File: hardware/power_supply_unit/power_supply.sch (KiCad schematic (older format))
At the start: 19 parts, among them U1 LT1074

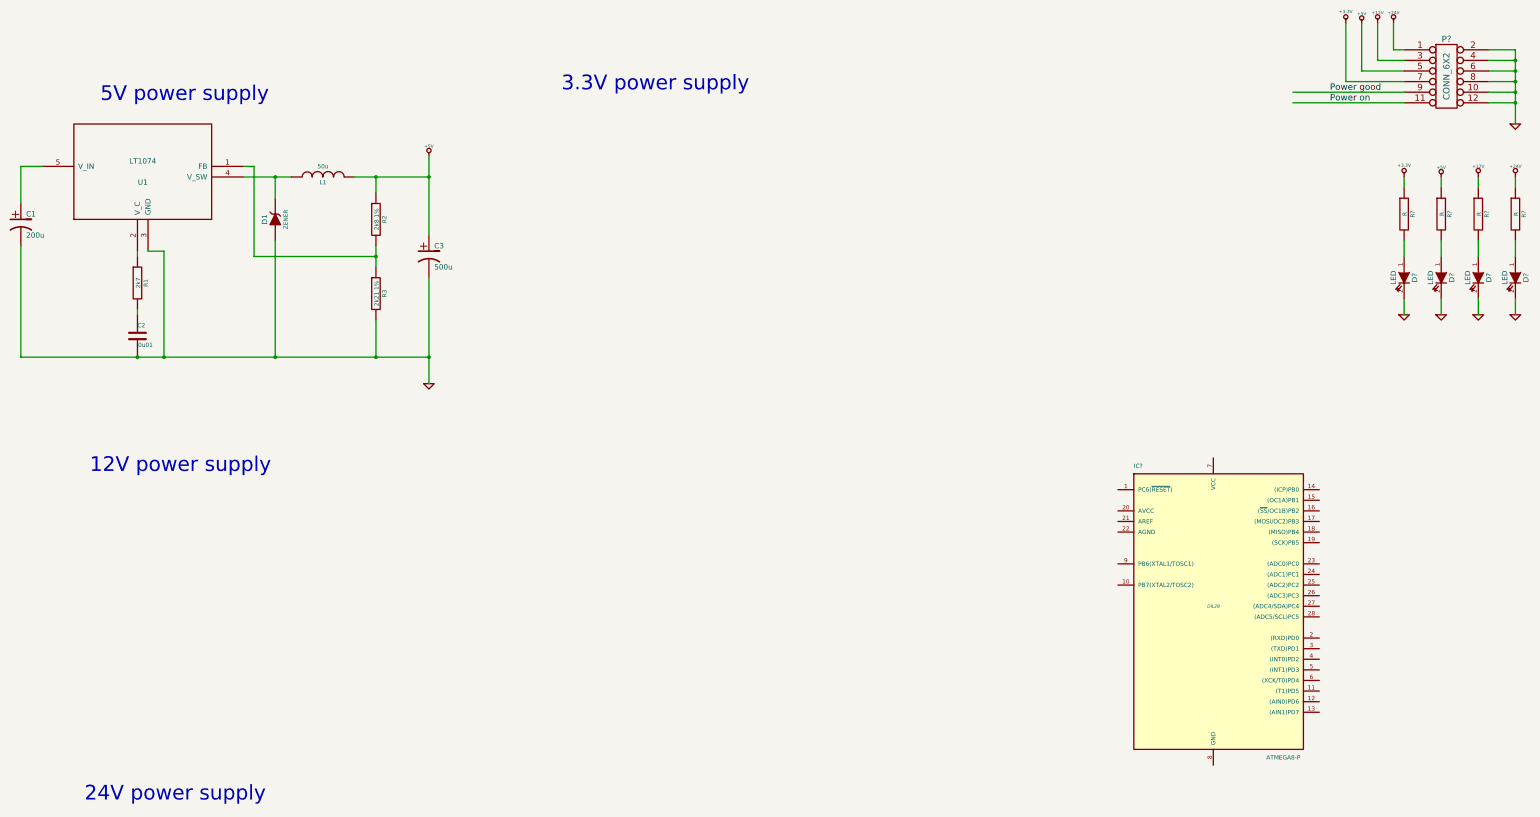
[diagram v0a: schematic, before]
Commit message: Improved digital output card with modbus controller
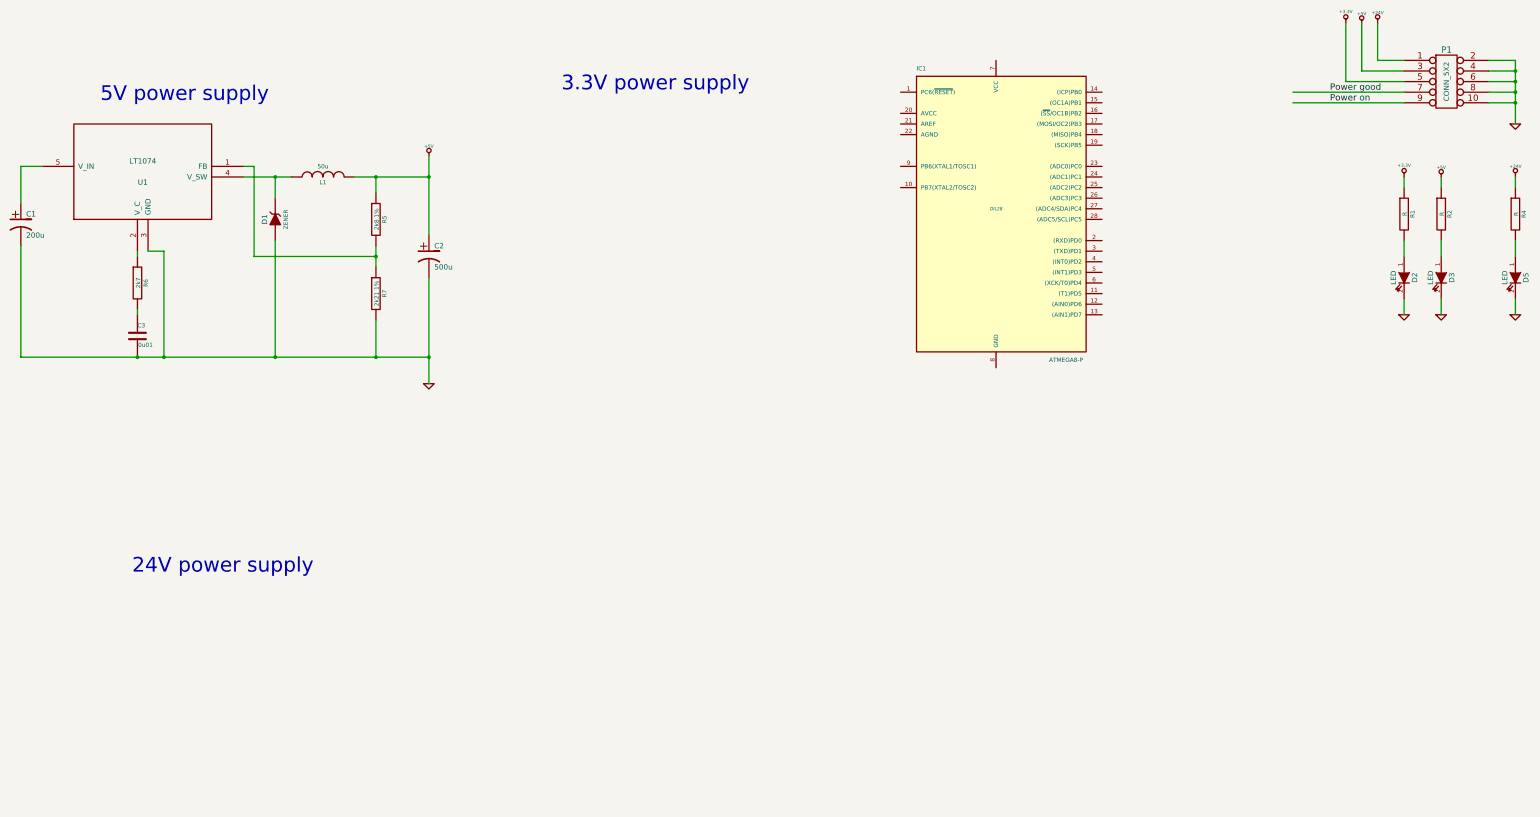
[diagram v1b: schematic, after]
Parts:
- removed D?: LED, ~, symbol LED
- removed P?: CONN_6X2, symbol CONN_6X2
- removed R?: R, ~, symbol R
- added P1: CONN_5X2, symbol CONN_5X2
- gave numbers to parts that had none: 7
- renumbered C3 to C2, C2 to C3, R2 to R5, R1 to R6, R3 to R7
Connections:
- net labels removed: +12V
- wire segments 49 -> 43
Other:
- note removed: "12V power supply"
- moved on the sheet: IC1
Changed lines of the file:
@@
 $EndComp
 $Comp
-L C C2
+L C C3
 U 1 1 5571A0D0
 P 2300 3850
-F 0 "C2" H 2300 3950 40  0000 L CNN
+F 0 "C3" H 2300 3950 40  0000 L CNN
 F 1 "0u01" H 2306 3765 40  0000 L CNN
 F 2 "~" H 2338 3700 30  0000 C CNN
@@
 Connection ~ 2300 4050
 $Comp
-L R R1
+L R R6
 U 1 1 5571A120
 P 2300 3350
-F 0 "R1" V 2380 3350 40  0000 C CNN
+F 0 "R6" V 2380 3350 40  0000 C CNN
 F 1 "2k7" V 2307 3351 40  0000 C CNN
 F 2 "~" V 2230 3350 30  0000 C CNN
@@
 Connection ~ 3600 2350
 $Comp
-L R R2
+L R R5
 U 1 1 5571A333
 P 4550 2750
-F 0 "R2" V 4630 2750 40  0000 C CNN
+F 0 "R5" V 4630 2750 40  0000 C CNN
 F 1 "2k8 1%" V 4557 2751 40  0000 C CNN
 F 2 "~" V 4480 2750 30  0000 C CNN
@@
 $EndComp
 $Comp
-L R R3
+L R R7
 U 1 1 5571A339
 P 4550 3450
-F 0 "R3" V 4630 3450 40  0000 C CNN
+F 0 "R7" V 4630 3450 40  0000 C CNN
 F 1 "2k21 1%" V 4557 3451 40  0000 C CNN
 F 2 "~" V 4480 3450 30  0000 C CNN
@@
 Connection ~ 3600 4050
 $Comp
-L CP1 C3
+L CP1 C2
 U 1 1 5571A3A1
 P 5050 3100
-F 0 "C3" H 5100 3200 50  0000 L CNN
+F 0 "C2" H 5100 3200 50  0000 L CNN
 F 1 "500u" H 5100 3000 50  0000 L CNN
 F 2 "~" H 5050 3100 60  0000 C CNN
@@
 Connection ~ 2550 4050
 $Comp
-L +5V #PWR?
+L +5V #PWR5
 U 1 1 5571A51F
 P 5050 2150
-F 0 "#PWR?" H 5050 2240 20  0001 C CNN
+F 0 "#PWR5" H 5050 2240 20  0001 C CNN
 F 1 "+5V" H 5050 2240 30  0000 C CNN
 F 2 "" H 5050 2150 60  0000 C CNN
@@
 Connection ~ 5050 2350
 $Comp
-L GND #PWR?
+L GND #PWR14
 U 1 1 5571A54A
 P 5050 4300
-F 0 "#PWR?" H 5050 4300 30  0001 C CNN
+F 0 "#PWR14" H 5050 4300 30  0001 C CNN
 F 1 "GND" H 5050 4230 30  0001 C CNN
 F 2 "" H 5050 4300 60  0000 C CNN
@@
 Text Notes 1950 1650 0    139  ~ 0
 5V power supply
-Text Notes 1850 5150 0    139  ~ 0
-12V power supply
-Text Notes 1800 8250 0    139  ~ 0
+Text Notes 2250 6100 0    139  ~ 0
 24V power supply
 Text Notes 6300 1550 0    139  ~ 0
 3.3V power supply
 $Comp
-L GND #PWR?
+L GND #PWR4
 U 1 1 5571A717
 P 15300 1850
-F 0 "#PWR?" H 15300 1850 30  0001 C CNN
+F 0 "#PWR4" H 15300 1850 30  0001 C CNN
 F 1 "GND" H 15300 1780 30  0001 C CNN
 F 2 "" H 15300 1850 60  0000 C CNN
@@
 	15300 1650 15050 1650
 Wire Wire Line
-	15300 1150 15300 1850
-Wire Wire Line
 	15050 1550 15300 1550
 Connection ~ 15300 1650
@@
 	15050 1350 15300 1350
 Connection ~ 15300 1450
-$Comp
-L CONN_6X2 P?
-U 1 1 5571A7CE
-P 14650 1400
-F 0 "P?" H 14650 1750 60  0000 C CNN
-F 1 "CONN_6X2" V 14650 1400 60  0000 C CNN
-F 2 "" H 14650 1400 60  0000 C CNN
-F 3 "" H 14650 1400 60  0000 C CNN
-	1    14650 1400
-	1    0    0    -1
-$EndComp
 Wire Wire Line
 	15050 1250 15300 1250
 Connection ~ 15300 1350
-Wire Wire Line
-	15050 1150 15300 1150
-Connection ~ 15300 1250
-$Comp
-L +24V #PWR?
+$Comp
+L +24V #PWR3
 U 1 1 5571A82B
-P 14150 900
-F 0 "#PWR?" H 14150 850 20  0001 C CNN
-F 1 "+24V" H 14150 1000 30  0000 C CNN
-F 2 "" H 14150 900 60  0000 C CNN
-F 3 "" H 14150 900 60  0000 C CNN
-	1    14150 900
-	1    0    0    -1
-$EndComp
-$Comp
-L +3,3V #PWR?
+P 14000 900
+F 0 "#PWR3" H 14000 850 20  0001 C CNN
+F 1 "+24V" H 14000 1000 30  0000 C CNN
+F 2 "" H 14000 900 60  0000 C CNN
+F 3 "" H 14000 900 60  0000 C CNN
+	1    14000 900
+	1    0    0    -1
+$EndComp
+$Comp
+L +3,3V #PWR1
 U 1 1 5571A83A
 P 13700 900
-F 0 "#PWR?" H 13700 860 30  0001 C CNN
+F 0 "#PWR1" H 13700 860 30  0001 C CNN
 F 1 "+3,3V" H 13700 1010 30  0000 C CNN
 F 2 "" H 13700 900 60  0000 C CNN
@@
 $EndComp
 $Comp
-L +12V #PWR?
-U 1 1 5571A858
-P 14000 900
-F 0 "#PWR?" H 14000 850 20  0001 C CNN
-F 1 "+12V" H 14000 1000 30  0000 C CNN
-F 2 "" H 14000 900 60  0000 C CNN
-F 3 "" H 14000 900 60  0000 C CNN
-	1    14000 900
-	1    0    0    -1
-$EndComp
-$Comp
-L +5V #PWR?
+L +5V #PWR2
 U 1 1 5571A885
 P 13850 900
-F 0 "#PWR?" H 13850 990 20  0001 C CNN
+F 0 "#PWR2" H 13850 990 20  0001 C CNN
 F 1 "+5V" H 13850 990 30  0000 C CNN
 F 2 "" H 13850 900 60  0000 C CNN
@@
 $EndComp
 Wire Wire Line
-	14150 900  14150 1150
-Wire Wire Line
-	14150 1150 14250 1150
-Wire Wire Line
 	14000 900  14000 1250
-Wire Wire Line
-	14000 1250 14250 1250
 Wire Wire Line
 	13850 900  13850 1350
@@
 Power good
 $Comp
-L +24V #PWR?
+L +24V #PWR9
 U 1 1 5571AA6C
 P 15300 2350
-F 0 "#PWR?" H 15300 2300 20  0001 C CNN
+F 0 "#PWR9" H 15300 2300 20  0001 C CNN
 F 1 "+24V" H 15300 2450 30  0000 C CNN
 F 2 "" H 15300 2350 60  0000 C CNN
@@
 $EndComp
 $Comp
-L +3,3V #PWR?
+L +3,3V #PWR6
 U 1 1 5571AA72
 P 14250 2350
-F 0 "#PWR?" H 14250 2310 30  0001 C CNN
+F 0 "#PWR6" H 14250 2310 30  0001 C CNN
 F 1 "+3,3V" H 14250 2460 30  0000 C CNN
 F 2 "" H 14250 2350 60  0000 C CNN
@@
 $EndComp
 $Comp
-L +12V #PWR?
-U 1 1 5571AA78
-P 14950 2350
-F 0 "#PWR?" H 14950 2300 20  0001 C CNN
-F 1 "+12V" H 14950 2450 30  0000 C CNN
-F 2 "" H 14950 2350 60  0000 C CNN
-F 3 "" H 14950 2350 60  0000 C CNN
-	1    14950 2350
-	1    0    0    -1
-$EndComp
-$Comp
-L +5V #PWR?
+L +5V #PWR7
 U 1 1 5571AA7E
 P 14600 2350
-F 0 "#PWR?" H 14600 2440 20  0001 C CNN
+F 0 "#PWR7" H 14600 2440 20  0001 C CNN
 F 1 "+5V" H 14600 2440 30  0000 C CNN
 F 2 "" H 14600 2350 60  0000 C CNN
@@
 $EndComp
 $Comp
-L R R?
+L R R1
 U 1 1 5571AA8A
 P 14250 2700
-F 0 "R?" V 14330 2700 40  0000 C CNN
+F 0 "R1" V 14330 2700 40  0000 C CNN
 F 1 "R" V 14257 2701 40  0000 C CNN
 F 2 "~" V 14180 2700 30  0000 C CNN
@@
 $EndComp
 $Comp
-L LED D?
+L LED D2
 U 1 1 5571AA99
 P 14250 3300
-F 0 "D?" H 14250 3400 50  0000 C CNN
+F 0 "D2" H 14250 3400 50  0000 C CNN
 F 1 "LED" H 14250 3200 50  0000 C CNN
 F 2 "~" H 14250 3300 60  0000 C CNN
@@
 $EndComp
 $Comp
-L GND #PWR?
+L GND #PWR10
 U 1 1 5571AAA8
 P 14250 3650
-F 0 "#PWR?" H 14250 3650 30  0001 C CNN
+F 0 "#PWR10" H 14250 3650 30  0001 C CNN
 F 1 "GND" H 14250 3580 30  0001 C CNN
 F 2 "" H 14250 3650 60  0000 C CNN
@@
 	14250 2350 14250 2450
 $Comp
-L R R?
+L R R2
 U 1 1 5571AB60
 P 14600 2700
-F 0 "R?" V 14680 2700 40  0000 C CNN
+F 0 "R2" V 14680 2700 40  0000 C CNN
 F 1 "R" V 14607 2701 40  0000 C CNN
 F 2 "~" V 14530 2700 30  0000 C CNN
@@
 $EndComp
 $Comp
-L LED D?
+L LED D3
 U 1 1 5571AB66
 P 14600 3300
-F 0 "D?" H 14600 3400 50  0000 C CNN
+F 0 "D3" H 14600 3400 50  0000 C CNN
 F 1 "LED" H 14600 3200 50  0000 C CNN
 F 2 "~" H 14600 3300 60  0000 C CNN
@@
 $EndComp
 $Comp
-L GND #PWR?
+L GND #PWR11
 U 1 1 5571AB6C
 P 14600 3650
-F 0 "#PWR?" H 14600 3650 30  0001 C CNN
+F 0 "#PWR11" H 14600 3650 30  0001 C CNN
 F 1 "GND" H 14600 3580 30  0001 C CNN
 F 2 "" H 14600 3650 60  0000 C CNN
@@
 	14600 2350 14600 2450
 $Comp
-L R R?
-U 1 1 5571AB75
-P 14950 2700
-F 0 "R?" V 15030 2700 40  0000 C CNN
-F 1 "R" V 14957 2701 40  0000 C CNN
-F 2 "~" V 14880 2700 30  0000 C CNN
-F 3 "~" H 14950 2700 30  0000 C CNN
-	1    14950 2700
-	1    0    0    -1
-$EndComp
-$Comp
-L LED D?
-U 1 1 5571AB7B
-P 14950 3300
-F 0 "D?" H 14950 3400 50  0000 C CNN
-F 1 "LED" H 14950 3200 50  0000 C CNN
-F 2 "~" H 14950 3300 60  0000 C CNN
-F 3 "~" H 14950 3300 60  0000 C CNN
-	1    14950 3300
-	0    1    1    0
-$EndComp
-$Comp
-L GND #PWR?
-U 1 1 5571AB81
-P 14950 3650
-F 0 "#PWR?" H 14950 3650 30  0001 C CNN
-F 1 "GND" H 14950 3580 30  0001 C CNN
-F 2 "" H 14950 3650 60  0000 C CNN
-F 3 "" H 14950 3650 60  0000 C CNN
-	1    14950 3650
-	1    0    0    -1
-$EndComp
-Wire Wire Line
-	14950 3650 14950 3500
-Wire Wire Line
-	14950 3100 14950 2950
-Wire Wire Line
-	14950 2350 14950 2450
-$Comp
-L R R?
+L R R4
 U 1 1 5571AB8A
 P 15300 2700
-F 0 "R?" V 15380 2700 40  0000 C CNN
+F 0 "R4" V 15380 2700 40  0000 C CNN
 F 1 "R" V 15307 2701 40  0000 C CNN
 F 2 "~" V 15230 2700 30  0000 C CNN
@@
 $EndComp
 $Comp
-L LED D?
+L LED D5
 U 1 1 5571AB90
 P 15300 3300
-F 0 "D?" H 15300 3400 50  0000 C CNN
+F 0 "D5" H 15300 3400 50  0000 C CNN
 F 1 "LED" H 15300 3200 50  0000 C CNN
 F 2 "~" H 15300 3300 60  0000 C CNN
@@
 $EndComp
 $Comp
-L GND #PWR?
+L GND #PWR13
 U 1 1 5571AB96
 P 15300 3650
-F 0 "#PWR?" H 15300 3650 30  0001 C CNN
+F 0 "#PWR13" H 15300 3650 30  0001 C CNN
 F 1 "GND" H 15300 3580 30  0001 C CNN
 F 2 "" H 15300 3650 60  0000 C CNN
@@
 	15300 2350 15300 2450
 $Comp
-L ATMEGA8-P IC?
+L ATMEGA8-P IC1
 U 1 1 5571AD07
-P 12450 6400
-F 0 "IC?" H 11700 7700 40  0000 L BNN
-F 1 "ATMEGA8-P" H 12950 4950 40  0000 L BNN
-F 2 "DIL28" H 12450 6400 30  0000 C CIN
-F 3 "" H 12450 6400 60  0000 C CNN
-	1    12450 6400
-	1    0    0    -1
-$EndComp
+P 10400 2650
+F 0 "IC1" H 9650 3950 40  0000 L BNN
+F 1 "ATMEGA8-P" H 10900 1200 40  0000 L BNN
+F 2 "DIL28" H 10400 2650 30  0000 C CIN
+F 3 "" H 10400 2650 60  0000 C CNN
+	1    10400 2650
+	1    0    0    -1
+$EndComp
+$Comp
+L CONN_5X2 P1
+U 1 1 5571DBE2
+P 14650 1450
+F 0 "P1" H 14650 1750 60  0000 C CNN
+F 1 "CONN_5X2" V 14650 1450 50  0000 C CNN
+F 2 "" H 14650 1450 60  0000 C CNN
+F 3 "" H 14650 1450 60  0000 C CNN
+	1    14650 1450
+	1    0    0    -1
+$EndComp
+Wire Wire Line
+	15300 1250 15300 1850
+Wire Wire Line
+	14000 1250 14250 1250
 $EndSCHEMATC
